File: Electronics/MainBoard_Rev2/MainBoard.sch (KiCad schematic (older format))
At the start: 27 parts, among them J1 Conn_01x04_Female, J2 DB9_Female, J5 Conn_01x02_Male, U1 ESP32-WROOM-32

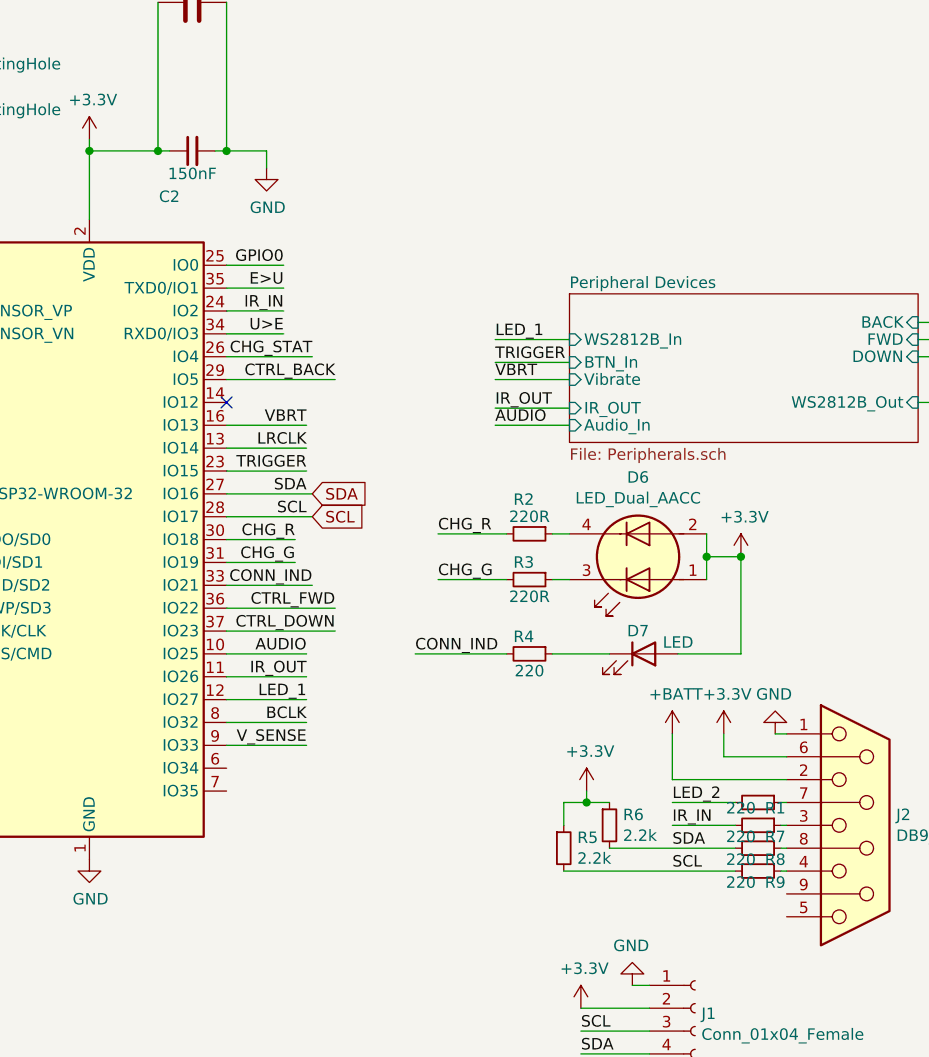
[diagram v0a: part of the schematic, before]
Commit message: Last changes for a functional Lasertag, ordered!
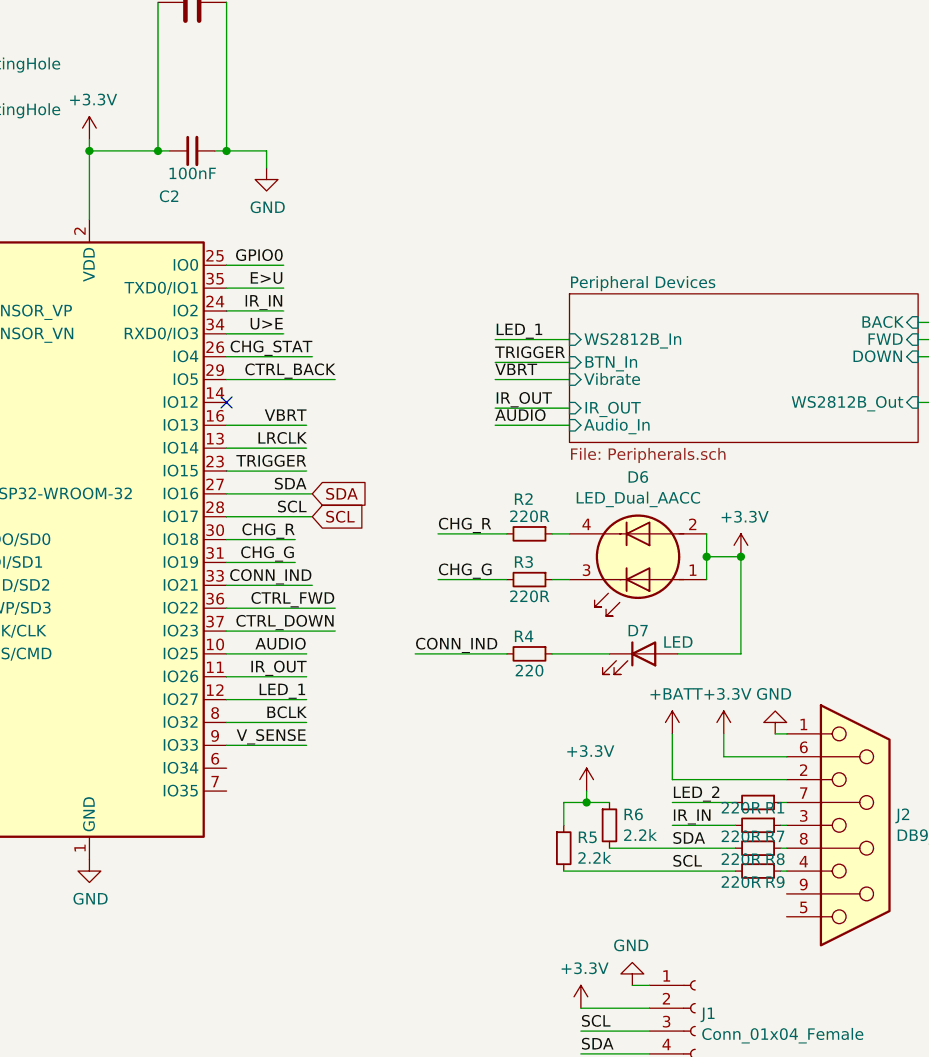
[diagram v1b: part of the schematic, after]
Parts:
- AMP1: Digi-Key_PN (none) -> MAX98357AETE+TCT-ND
- C2: value 150nF -> 100nF
- D6: Digi-Key 160-1172-1-ND -> (none); Digi-Key_PN (none) -> 160-1172-1-ND
- D7: Digi-Key 1830-1068-1-ND -> (none); Digi-Key_PN (none) -> 1830-1068-1-ND
- J2: Digi-Key AE10921-ND -> (none); Digi-Key_PN (none) -> AE10921-ND
- J5: Digi-Key_PN (none) -> 668-1517-ND
- R1, R7, R8, R9: value 220 -> 220R
- U1: Digi-Key 1904-1025-1-ND -> (none); Digi-Key_PN (none) -> 1904-1025-1-ND
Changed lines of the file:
@@
 F 2 "RF_Module:ESP32-WROOM-32" H 5950 2000 50  0001 C CNN
 F 3 "https://www.espressif.com/sites/default/files/documentation/esp32-wroom-32_datasheet_en.pdf" H 5650 3550 50  0001 C CNN
-F 4 "1904-1025-1-ND" H 5950 3500 50  0001 C CNN "Digi-Key"
+F 4 "1904-1025-1-ND" H 5950 3500 50  0001 C CNN "Digi-Key_PN"
 F 5 "ESP32-WROOM-32D (16MB)" H 5950 3500 50  0001 C CNN "MPN"
 	1    5950 3500
@@
 P 6400 1800
 F 0 "C2" V 6200 1900 50  0000 C CNN
-F 1 "150nF" V 6300 1800 50  0000 C CNN
+F 1 "100nF" V 6300 1800 50  0000 C CNN
 F 2 "Capacitor_SMD:C_0805_2012Metric" H 6400 1800 50  0001 C CNN
 F 3 "~" H 6400 1800 50  0001 C CNN
@@
 F 2 "Connector_Dsub:DSUB-9_Female_Horizontal_P2.77x2.84mm_EdgePinOffset4.94mm_Housed_MountingHolesOffset7.48mm" H 9300 4750 50  0001 C CNN
 F 3 " ~" H 9300 4750 50  0001 C CNN
-F 4 "AE10921-ND" H 9300 4750 50  0001 C CNN "Digi-Key"
+F 4 "AE10921-ND" H 9300 4750 50  0001 C CNN "Digi-Key_PN"
 F 5 "A-DF 09 A/KG-T2S" H 9300 4750 50  0001 C CNN "MPN"
 	1    9300 4750
@@
 F 2 "LED_SMD:LED_0603_1608Metric" H 8375 4000 50  0001 C CNN
 F 3 "~" H 8375 4000 50  0001 C CNN
-F 4 "1830-1068-1-ND" H 8375 4000 50  0001 C CNN "Digi-Key"
+F 4 "1830-1068-1-ND" H 8375 4000 50  0001 C CNN "Digi-Key_PN"
 F 5 "IN-S63BT5B" H 8375 4000 50  0001 C CNN "MPN"
 	1    8375 4000
@@
 F 2 "LED_SMD:LED_RGB_1210" H 8350 3320 50  0001 C CNN
 F 3 "~" H 8380 3575 50  0001 C CNN
-F 4 "160-1172-1-ND" H 8350 3575 50  0001 C CNN "Digi-Key"
+F 4 "160-1172-1-ND" H 8350 3575 50  0001 C CNN "Digi-Key_PN"
 F 5 "LTST-C155GEKT" H 8350 3575 50  0001 C CNN "MPN"
 	1    8350 3575
@@
 F 2 "Package_DFN_QFN:QFN-16-1EP_3x3mm_P0.5mm_EP2.7x2.7mm_ThermalVias" H 4025 5900 50  0001 C CNN
 F 3 "" H 4025 5900 50  0001 C CNN
+F 4 "MAX98357AETE+TCT-ND" H 3925 6250 50  0001 C CNN "Digi-Key_PN"
 	1    3925 6250
 	1    0    0    -1
@@
 P 8875 4650
 F 0 "R1" V 8900 4725 50  0000 C CNN
-F 1 "220" V 8900 4575 50  0000 C CNN
+F 1 "220R" V 8900 4575 50  0000 C CNN
 F 2 "Resistor_SMD:R_0805_2012Metric" H 8875 4650 50  0001 C CNN
 F 3 "~" H 8875 4650 50  0001 C CNN
@@
 P 8875 4750
 F 0 "R7" V 8925 4825 50  0000 C CNN
-F 1 "220" V 8925 4675 50  0000 C CNN
+F 1 "220R" V 8925 4675 50  0000 C CNN
 F 2 "Resistor_SMD:R_0805_2012Metric" H 8875 4750 50  0001 C CNN
 F 3 "~" H 8875 4750 50  0001 C CNN
@@
 F 2 "Connector_PinHeader_2.00mm:PinHeader_1x02_P2.00mm_Vertical" H 4925 5900 50  0001 C CNN
 F 3 "~" H 4925 5900 50  0001 C CNN
+F 4 "668-1517-ND" H 4925 5900 50  0001 C CNN "Digi-Key_PN"
 	1    4925 5900
 	-1   0    0    1
@@
 P 8875 4850
 F 0 "R8" V 8925 4925 50  0000 C CNN
-F 1 "220" V 8925 4775 50  0000 C CNN
+F 1 "220R" V 8925 4775 50  0000 C CNN
 F 2 "Resistor_SMD:R_0805_2012Metric" H 8875 4850 50  0001 C CNN
 F 3 "~" H 8875 4850 50  0001 C CNN
@@
 P 8875 4950
 F 0 "R9" V 8925 5025 50  0000 C CNN
-F 1 "220" V 8925 4875 50  0000 C CNN
+F 1 "220R" V 8925 4875 50  0000 C CNN
 F 2 "Resistor_SMD:R_0805_2012Metric" H 8875 4950 50  0001 C CNN
 F 3 "~" H 8875 4950 50  0001 C CNN

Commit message: Modify board for the v3.3 release-ish
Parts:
- removed D6: LED_Dual_AACC, LED_SMD:LED_RGB_1210, symbol Device:LED_Dual_AACC
- removed D7: LED, LED_SMD:LED_0603_1608Metric, symbol Device:LED
- removed J2: DB9_Female, Connector_Dsub:DSUB-9_Female_Horizontal_P2.77x2.84mm_EdgePinOffset4.94mm_Housed_MountingHolesOffset7.48mm, symbol Connector:DB9_Female
- removed R2, R3: 220R, Resistor_SMD:R_0805_2012Metric, symbol Device:R_Small
- removed R4: 220, Resistor_SMD:R_0805_2012Metric, symbol Device:R_Small
- added J101: 54602-908LF, Connector_RJ:RJ45_Amphenol_54602-x08_Horizontal, symbol Connector:RJ45
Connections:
- net +3V3: now also J101.3
- net +BATT: now also AMP1.7 (Vdd), J101.2
- net GND: now also J101.1
- net at R7.1: now also J101.6
- net at R9.1: now also J101.7
- net at R1.1: now also J101.5
- net at R8.1: now also J101.8
- net CHG_G: no longer names the net of U1.31 (IO19)
- net CHG_R: no longer names the net of U1.30 (IO18)
- net CONN_IND: no longer names the net of U1.33 (IO21)
- net VBRT: no longer names the net of U1.16 (IO13)
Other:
- note added: "Digi-Key PN for cable:\nA3882R-05C-ND"
- note added: "Known passives:\n- 10k\n- 50k better tolerance\n- 2.2k\n- 220Ω\n\nCapacities:\n- 0.1uF\n- 1uF\n- 10uF\n- >22uF (1206)"
- moved on the sheet: R1, R5, R6, R7, R8, R9
